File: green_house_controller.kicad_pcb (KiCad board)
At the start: 2 copper layers, 103.1 x 76.2 mm, 110 parts, among them J1 TC2030-IDC, J2 Screw_Terminal_01x10, J3 USB_B_Mini, J4 Screw_Terminal_01x06, J5 Screw_Terminal_01x03, J6 Barrel_Jack, Q1 2N7002, Q10 DMG3406L, Q11 DMP3068L, Q12 DMG3406L, Q13 2N7002, Q14 DMP3068L, Q15 DMG3406L, Q16 DMP3068L, Q17 DMG3406L, Q19 2N7002, Q2 2N7002, Q3 DMP3068L, Q4 DMG3406L, Q5 DMP3068L, Q6 DMG3406L, Q7 2N7002, Q8 2N7002, Q9 DMP3068L, SW1 SW_Push, U1 ESP32-WROVER, U2 TPS54231, U3 TLP3825TP1_F, U4 TLP3825TP1_F, U5 TLP3825TP1_F, U6 TLP3825TP1_F, U7 LM2733XMF

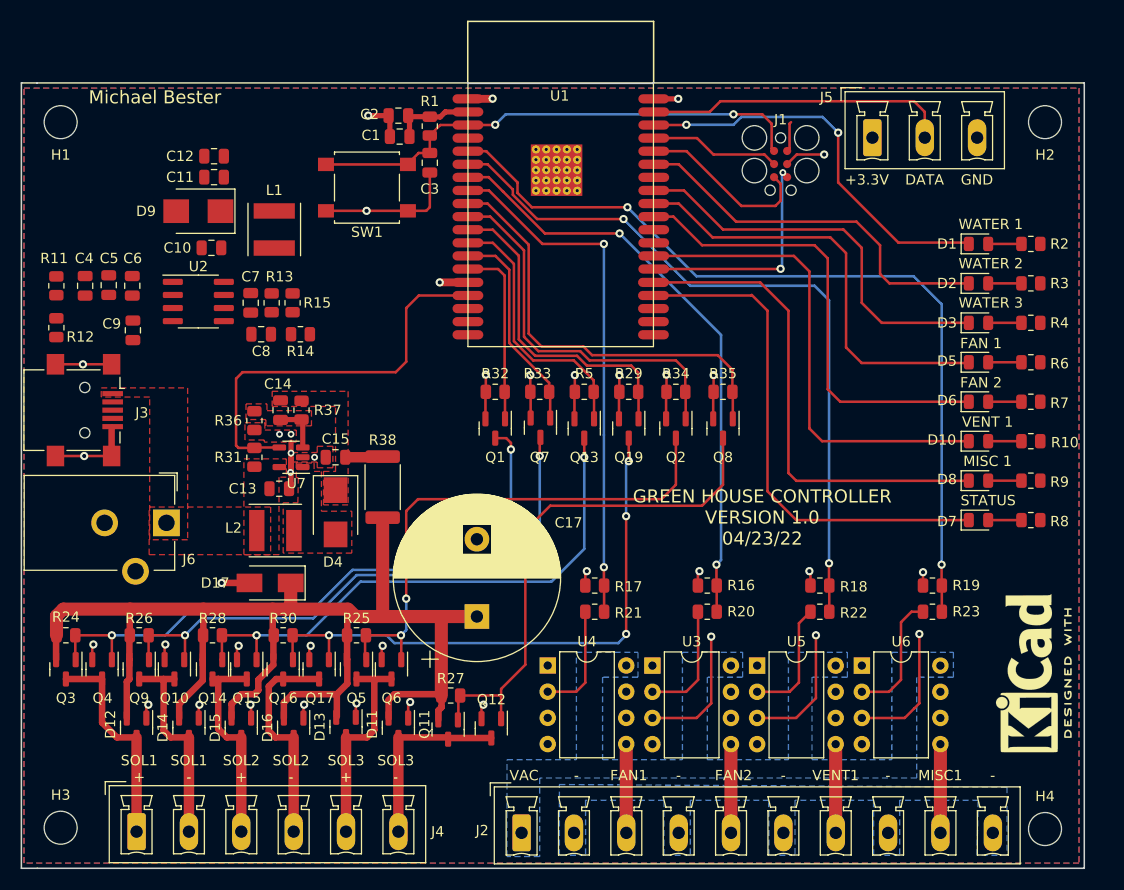
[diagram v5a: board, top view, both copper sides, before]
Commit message: Finished initial layout.  Zero DRC errors/warnings.
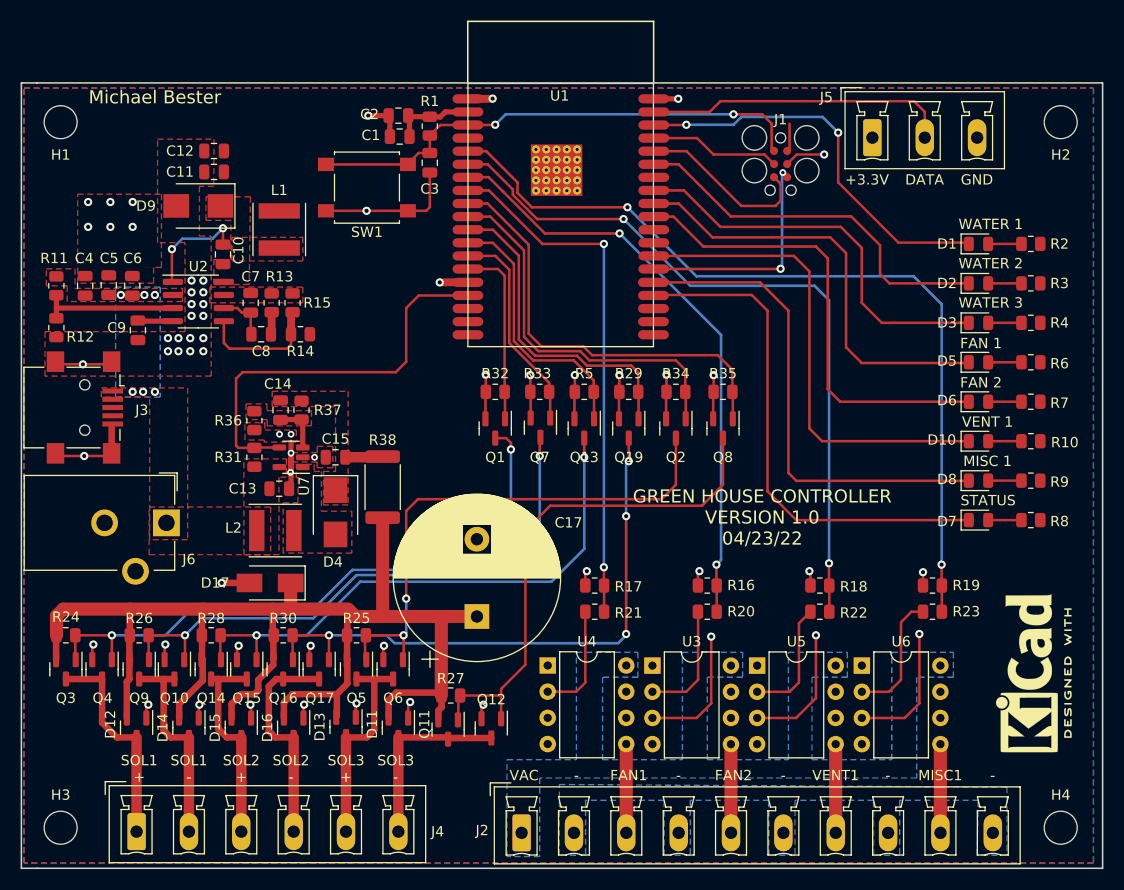
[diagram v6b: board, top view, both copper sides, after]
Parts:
- moved H4 1.53 mm to (199.4, 130.0)
- moved H2 1.52 mm to (199.4, 61.6)
- moved C10 1.29 mm to (118.1, 74.4), turned to -90 degrees
- moved C12 0.51 mm to (117.2, 64.4)
- moved C11 0.51 mm to (117.2, 66.4)
- moved D9 0.51 mm to (115.7, 69.7)
- moved C9 0.48 mm to (109.9, 81.8)
- moved L1 0.48 mm to (123.6, 72.0)
- moved J3 0.25 mm to (104.7, 89.3)
- moved Q6 0.16 mm to (134.6, 114.7)
- moved Q14 0.13 mm to (117.0, 114.7)
- moved R28 0.13 mm to (117.0, 111.4)
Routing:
- net Net-(R11-Pad2): track 0.00 -> 13.6 mm
- net Net-(R14-Pad2): track 0.00 -> 12.2 mm
- net Net-(C10-Pad1): track 0.00 -> 11.0 mm, vias 0 -> 2
- net Net-(C7-Pad1): track 0.00 -> 4.91 mm
- net Net-(C9-Pad1): track 0.00 -> 3.26 mm
- net Net-(C8-Pad2): track 0.00 -> 2.16 mm
- net GND: track 140.1 -> 138.2 mm, vias 39 -> 61
- net /power supply/VIN: vias 0 -> 6
- added copper zone on B.Cu, net /power supply/VIN
- added copper zone on F.Cu, net Net-(C10-Pad2)
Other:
- board size 103.1 x 76.2 mm -> 104.9 x 76.2 mm

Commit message: Added DHT11 footprint. Updated feedback resistor values for regulator circuit. Created gerber and drill files for version 1.
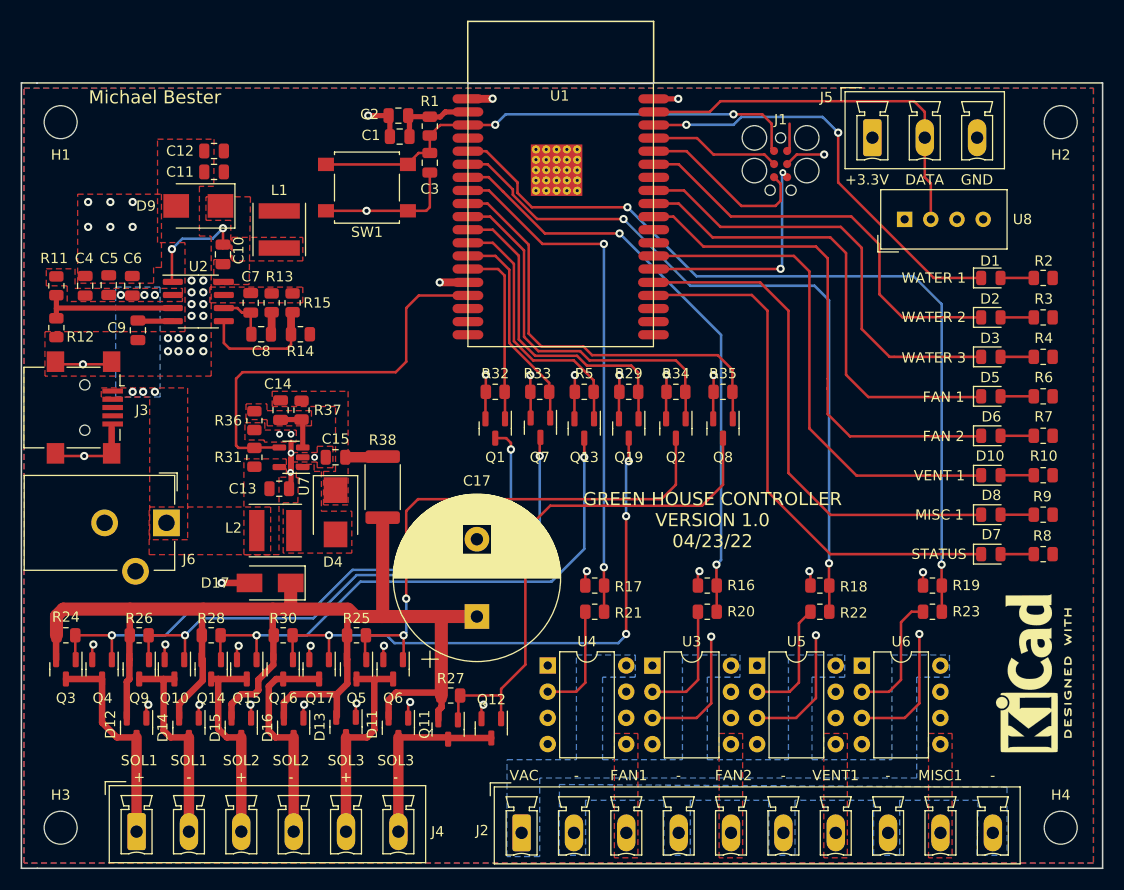
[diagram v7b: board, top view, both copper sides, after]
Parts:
- added U8: DHT11, Sensor:Aosong_DHT11_5.5x12.0_P2.54mm, F.Cu at (184.2, 71.0)
- R11: value 150K -> 22K
- R12: value 5.36K -> 10K
- R37: value 1K -> 18.7K
- moved D1 3.51 mm to (192.6, 76.7)
- moved D10 3.51 mm to (192.6, 95.8)
- moved D2 3.51 mm to (192.6, 80.5)
- moved D3 3.51 mm to (192.6, 84.4)
- moved D5 3.51 mm to (192.6, 88.2)
- moved D6 3.51 mm to (192.6, 92.0)
- moved D7 3.51 mm to (192.6, 103.5)
- moved D8 3.51 mm to (192.6, 99.7)
- moved R10 3.51 mm to (197.7, 95.8)
- moved R2 3.51 mm to (197.7, 76.7)
- moved R3 3.51 mm to (197.7, 80.5)
- moved R4 3.51 mm to (197.7, 84.4)
- moved R6 3.51 mm to (197.7, 88.2)
- moved R7 3.51 mm to (197.7, 92.0)
- moved R8 3.51 mm to (197.7, 103.5)
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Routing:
- net /relay control/FAN_1_PWR: track 8.62 -> 0.00 mm
- net /relay control/FAN_2_PWR: track 8.61 -> 0.00 mm
- net /relay control/VENT_1_PWR: track 8.61 -> 0.00 mm
- net /relay control/MISC_1_PWR: track 8.61 -> 0.00 mm
- net /microcontroller/DHT11_DATA: track 29.7 -> 37.8 mm
- net /microcontroller/LED_FAN_2: track 45.4 -> 49.6 mm
- net /microcontroller/LED_FAN_1: track 42.4 -> 46.5 mm
- net /microcontroller/LED_SOL_3: track 39.0 -> 43.1 mm
- net /microcontroller/LED_SOL_2: track 37.0 -> 40.7 mm
- net /microcontroller/LED_VENT_1: track 46.9 -> 49.5 mm
- net /microcontroller/LED_SOL_1: track 38.8 -> 41.4 mm
- net /microcontroller/LED_STATUS: track 49.9 -> 52.5 mm
- net /microcontroller/LED_MISC_1: track 47.8 -> 50.4 mm
- added copper zone on F.Cu, net /relay control/FAN_1_PWR
- added copper zone on F.Cu, net /relay control/FAN_2_PWR
- added copper zone on F.Cu, net /relay control/MISC_1_PWR
- added copper zone on F.Cu, net /relay control/VENT_1_PWR

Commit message: Fixed 3.3V net disconnection issue.
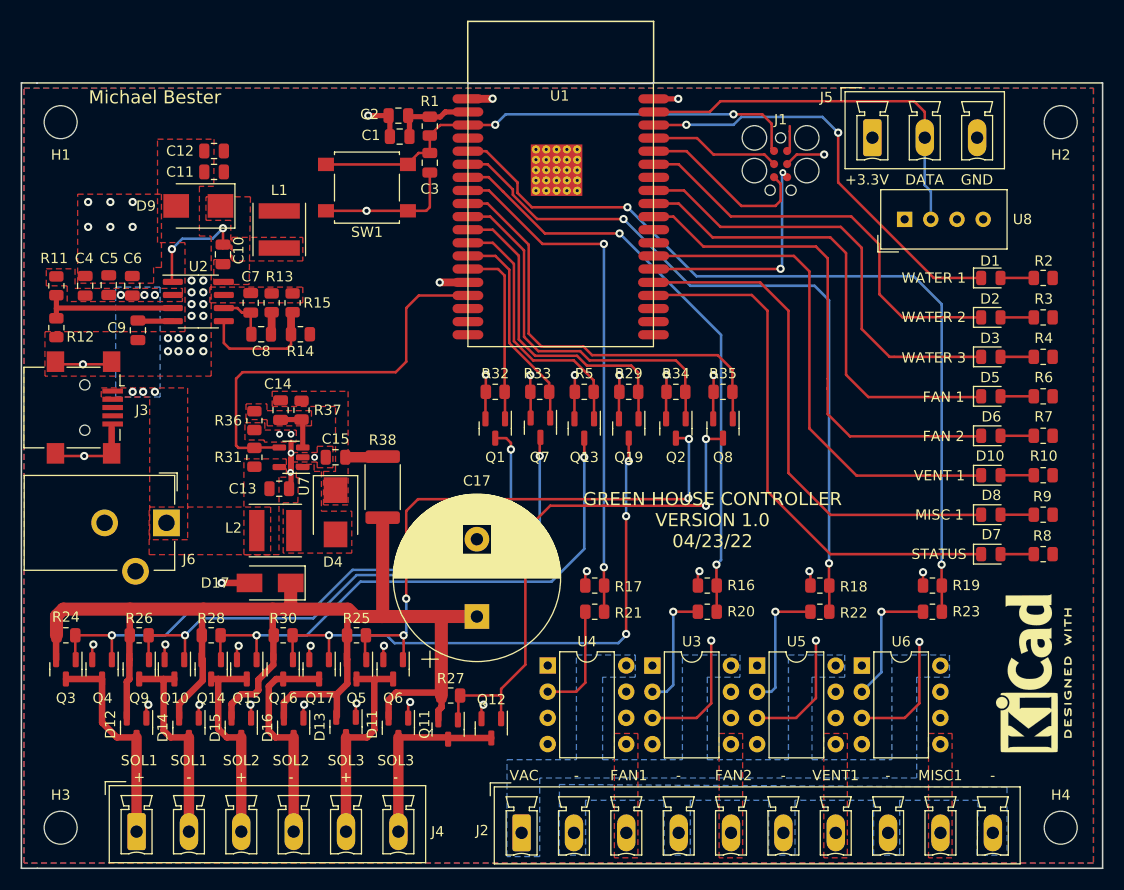
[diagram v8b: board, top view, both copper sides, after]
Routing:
- net Net-(Q2-Pad3): track 52.4 -> 55.7 mm, vias 2 -> 4
- net Net-(Q11-Pad1): track 51.2 -> 53.5 mm, vias 0 -> 2
- net GND: track 138.2 -> 136.6 mm
- net Net-(R22-Pad1): track 11.8 -> 12.7 mm, vias 0 -> 1
- net Net-(R20-Pad1): track 11.5 -> 11.8 mm, vias 0 -> 1
- net Net-(R23-Pad1): track 12.4 -> 12.6 mm, vias 0 -> 1
